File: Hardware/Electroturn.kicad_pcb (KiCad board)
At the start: 2 copper layers, 122 x 83.1 mm, 45 parts, among them Q1 2N2222, U2 RT9193-3.3, U3 74HC4050D

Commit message: Something like a pcb?
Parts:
- removed @HOLE0, @HOLE1, @HOLE2, @HOLE3: , 
- removed A0, A1, A2: , Adafruit 0.54 Alphanumeric v0.1:SOLDERJUMPER_REFLOW_NOPASTE
- removed C1: 10uF, Adafruit 0.54 Alphanumeric v0.1:0805-NO
- removed C1, C2, C3: 10uF, Adafruit_2.2_SPI_240x320:_0805MP
- removed CN1: , Adafruit_2.2_SPI_240x320:MICROSD
- removed D1: 1N4148, Adafruit 0.54 Alphanumeric v0.1:SOD-323F
- removed FID1, FID2, FID3: FIDUCIAL"", Adafruit_2.2_SPI_240x320:FIDUCIAL_1MM
- removed JP1: , Adafruit 0.54 Alphanumeric v0.1:1X05_ROUND_70
- removed JP1: , Adafruit_2.2_SPI_240x320:1X10_ROUND70
- removed LED1, LED2: , Adafruit 0.54 Alphanumeric v0.1:SEGMENT_STARTBUST_DUAL_KWA-541CBB
- removed Q1: 2N2222, Adafruit_2.2_SPI_240x320:SOT23-WIDE
- removed R1, R2: 10K, Adafruit 0.54 Alphanumeric v0.1:0805-NO
- removed R1, R2, R3, R6: 10, Adafruit_2.2_SPI_240x320:_0805MP
- removed R3, R4, R5: 47K, Adafruit 0.54 Alphanumeric v0.1:0805-NO
- removed R4: 1K, Adafruit_2.2_SPI_240x320:_0805MP
- removed R5: 10K, Adafruit_2.2_SPI_240x320:_0805MP
- removed U$1, U$2: FIDUCIAL, Adafruit 0.54 Alphanumeric v0.1:FIDUCIAL_1MM
- removed U$2, U$3, U$4, U$5: MOUNTINGHOLE2.5, Adafruit_2.2_SPI_240x320:MOUNTINGHOLE_2.5_PLATED
- removed U$20: , Adafruit_2.2_SPI_240x320:ADAFRUIT_TEXT_30MM
- removed U$3: , Adafruit 0.54 Alphanumeric v0.1:ADAFRUIT_9MM
- removed U1: , Adafruit_2.2_SPI_240x320:TM022HDH26_2.2IN_LCD
- removed U2: , Adafruit 0.54 Alphanumeric v0.1:SOP28_300MIL
- removed U2: RT9193-3.3, Adafruit_2.2_SPI_240x320:SOT23-5
- removed U3: 74HC4050D, Adafruit_2.2_SPI_240x320:SOIC16
- added REF**: Gecko G250x, Connector_PinSocket_2.54mm:PinSocket_2x15_P2.54mm_Vertical, F.Cu at (99.1, 78.7)
- added REF**: Alphanumeric, Connector_PinSocket_2.54mm:PinSocket_1x05_P2.54mm_Vertical, F.Cu at (121.9, 38.1)
- added REF**: Screw Terminal, TerminalBlock_Wuerth:Wuerth_REDCUBE-THR_WP-THRBU_74650194_THR, F.Cu at (118.0, 110.0)
- added REF**: 5k, Resistor_SMD:R_0402_1005Metric, F.Cu at (117.3, 56.6)
- added REF**: Screw Terminal, TerminalBlock_Wuerth:Wuerth_REDCUBE-THR_WP-THRBU_74650194_THR, F.Cu at (94.0, 45.7)
- added REF**: 10k, Resistor_SMD:R_0402_1005Metric, F.Cu at (107.2, 61.7)
- added REF**: 5k, Resistor_SMD:R_0402_1005Metric, F.Cu at (117.3, 61.6)
- added REF**: TFT Display, Connector_PinSocket_2.54mm:PinSocket_1x10_P2.54mm_Vertical, F.Cu at (172.1, 64.2)
- added REF**: 10k, Resistor_SMD:R_0402_1005Metric, F.Cu at (107.2, 56.6)
- added REF**: 2.8k, Resistor_SMD:R_0402_1005Metric, F.Cu at (89.5, 109.0)
- moved REF** 54.1 mm to (137.6, 77.2)
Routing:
- net (no net): track 1691.0 -> 1259.2 mm, vias 51 -> 40
- removed copper zone on F.Cu, net (none)
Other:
- board size 122 x 83.1 mm -> 100 x 100 mm
- board text removed: "+"
- board text removed: "-"
- board text removed: "0.54" 14-segment LED HT16K33 Backpack"
- board text removed: "240x320 2.2" TFT w/ILI9340C"
- board text removed: "A0"
- board text removed: "A1"
- board text removed: "A2"
- board text removed: "BACKLIGHT"
- board text removed: "BL"
- board text removed: "Backlight: PWM Safe"
- board text removed: "C"
- board text removed: "CS"
- board text removed: "D"
- board text removed: "D/C"
- board text removed: "GND"
- board text removed: "LCD CS"
- board text removed: "Logic: 3.3-5V"
- board text removed: "MISO"
- board text removed: "MOSI"
- board text removed: "RESET"
- board text removed: "RST"
- board text removed: "SCK"
- board text removed: "SCL"
- board text removed: "SD CS"
- board text removed: "SDA"
- board text removed: "SDCS"
- board text removed: "VCC"
- board text removed: "VIN"
- board text removed: "VIN: 3.3-5V"
- board text removed: "Vi2c"
- board text removed: "by adafruit!"

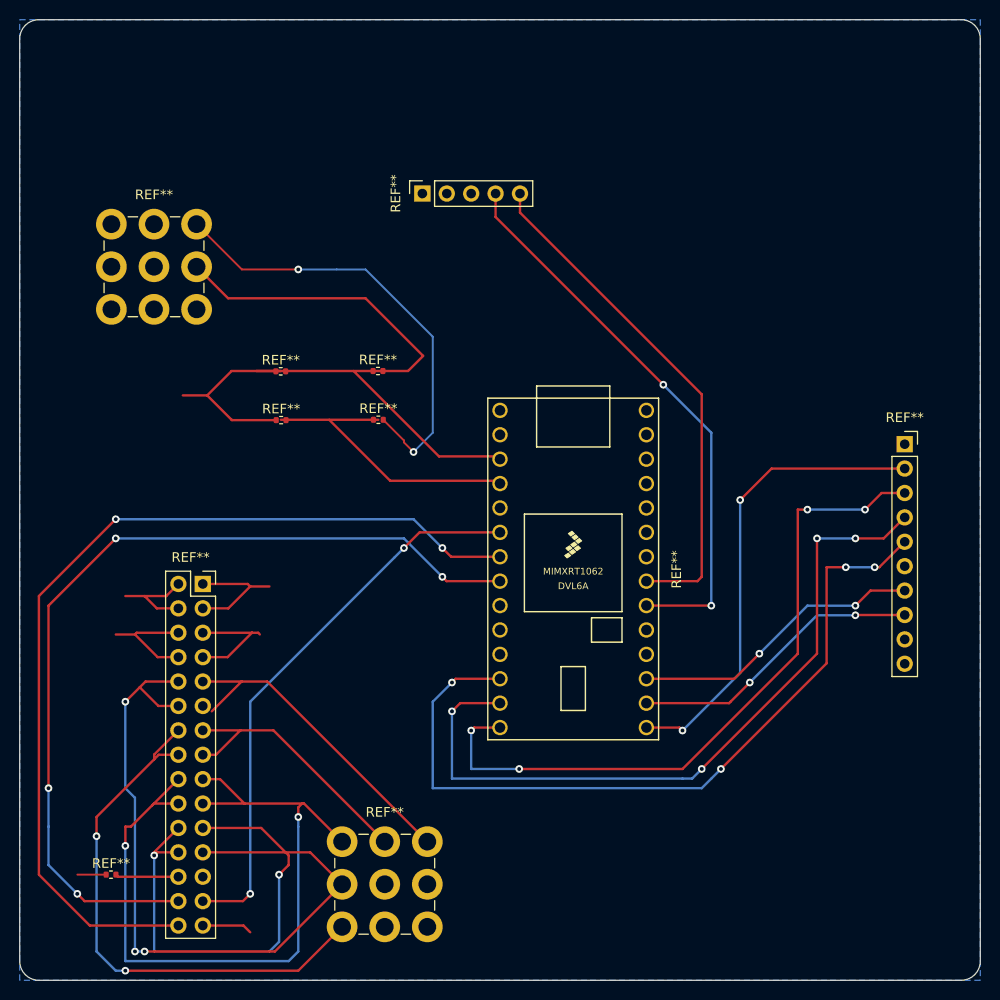
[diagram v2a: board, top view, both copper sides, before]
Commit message: Reorganizing KiCAD repo, fixing path issues
I tidied up the folder structure, and also went in and relinked all the footprints/symbols using the correct new paths. Should work across any system now. Also linked the appropriate 3D models for the Teensy and Gecko.
I updated the PCB to include all these new changes from the footprints/schematic, and in doing so it pretty much destroyed what Karson had...sorry Karson
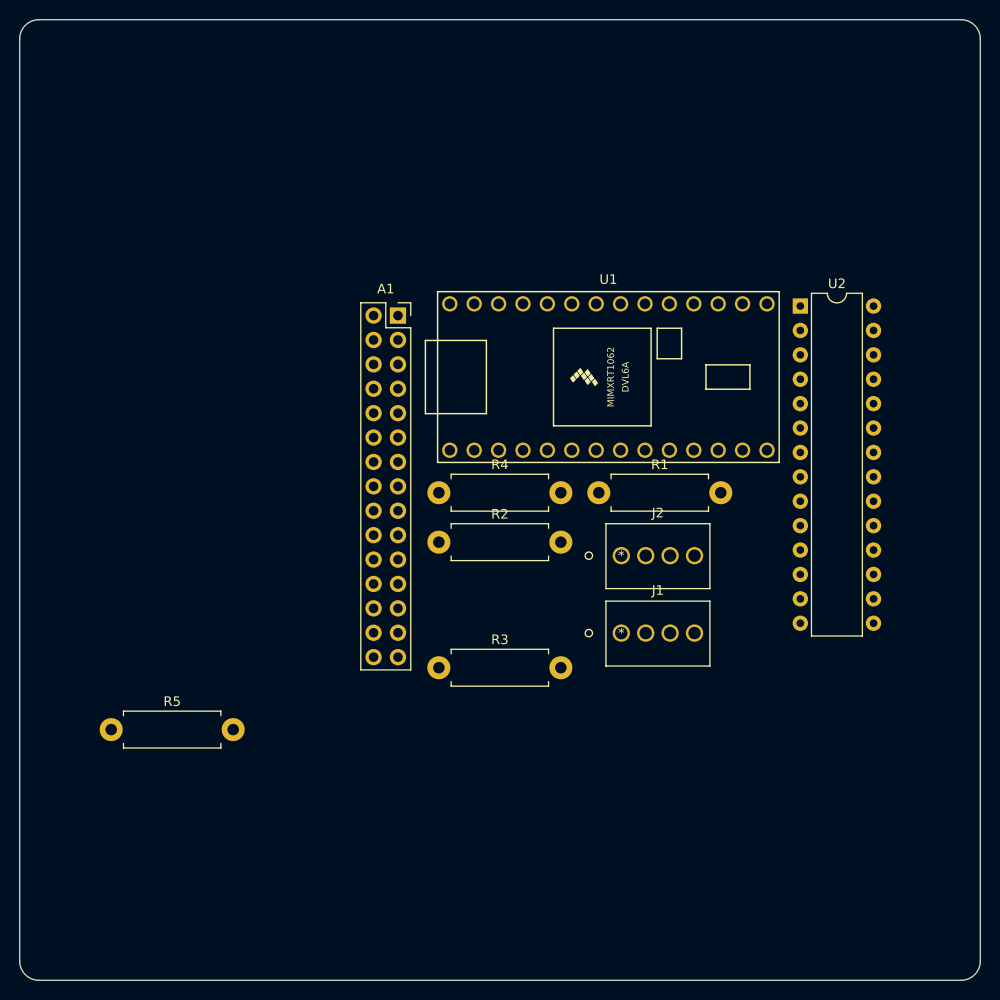
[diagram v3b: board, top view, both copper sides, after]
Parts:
- removed REF**: Gecko G250x, Connector_PinSocket_2.54mm:PinSocket_2x15_P2.54mm_Vertical
- removed REF**: Alphanumeric, Connector_PinSocket_2.54mm:PinSocket_1x05_P2.54mm_Vertical
- removed REF** (x2): Screw Terminal, TerminalBlock_Wuerth:Wuerth_REDCUBE-THR_WP-THRBU_74650194_THR
- removed REF** (x2): 5k, Resistor_SMD:R_0402_1005Metric
- removed REF** (x2): 10k, Resistor_SMD:R_0402_1005Metric
- removed REF**: TFT Display, Connector_PinSocket_2.54mm:PinSocket_1x10_P2.54mm_Vertical
- removed REF**: 2.8k, Resistor_SMD:R_0402_1005Metric
- removed REF**: Teensy 4.0, teensy:Teensy40
- added A1: Gecko G250X, Electroturn_Parts:GeckoG250XR2_WithHeatsink, F.Cu at (119.4, 50.8)
- added J1: Encoder Terminal, Electroturn_Parts:ScrewTerminal4_OSTVN04A150, F.Cu at (142.6, 83.9)
- added J2: Stepper Motor Terminal, Electroturn_Parts:ScrewTerminal4_OSTVN04A150, F.Cu at (142.6, 75.8)
- added R1: 10k, Resistor_THT:R_Axial_DIN0411_L9.9mm_D3.6mm_P12.70mm_Horizontal, F.Cu at (140.3, 69.2)
- added R2: 10k, Resistor_THT:R_Axial_DIN0411_L9.9mm_D3.6mm_P12.70mm_Horizontal, F.Cu at (123.6, 74.4)
- added R3: 5k, Resistor_THT:R_Axial_DIN0411_L9.9mm_D3.6mm_P12.70mm_Horizontal, F.Cu at (123.6, 87.5)
- added R4: 5k, Resistor_THT:R_Axial_DIN0411_L9.9mm_D3.6mm_P12.70mm_Horizontal, F.Cu at (123.6, 69.2)
- added R5: 2.8K, Resistor_THT:R_Axial_DIN0411_L9.9mm_D3.6mm_P12.70mm_Horizontal, F.Cu at (89.5, 93.9)
- added U1: Teensy 4.0, Electroturn_Parts:Teensy40_OnFemaleHeaders, F.Cu at (141.3, 57.2)
- added U2: MCP23017_SP, Package_DIP:DIP-28_W7.62mm, F.Cu at (161.3, 49.8)
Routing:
- net (no net): track 1259.2 -> 0.00 mm, vias 40 -> 0
- removed copper zone on B.Cu, net (none)

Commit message: Initial PCB work
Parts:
- added C1: 0.01uF, Capacitor_THT:C_Disc_D9.0mm_W5.0mm_P7.50mm, B.Cu at (195.8, 190.2)
- added C2: 0.01uF, Capacitor_THT:C_Disc_D9.0mm_W5.0mm_P7.50mm, B.Cu at (88.3, 159.4)
- added D1: Spindle Overspeed LED, LED_THT:LED_D5.0mm, F.Cu at (137.8, 73.7)
- added DS1: Adafruit_1002_Alphanumeric, Electroturn_Parts:Adafruit1002_0.54inAlphanumericBackpack, F.Cu at (121.9, 39.6)
- added DS2: Adafruit_1480_2.2inTFT, Electroturn_Parts:Adafruit1480_TFTwithHeaders, F.Cu at (160.7, 112.1)
- added R10: 10k, Resistor_THT:R_Axial_DIN0411_L9.9mm_D3.6mm_P12.70mm_Horizontal, B.Cu at (59.8, 147.3)
- added R11: 10k, Resistor_THT:R_Axial_DIN0411_L9.9mm_D3.6mm_P12.70mm_Horizontal, B.Cu at (177.3, 163.8)
- added R6: 1.5k, Resistor_THT:R_Axial_DIN0411_L9.9mm_D3.6mm_P12.70mm_Horizontal, B.Cu at (177.3, 168.9)
- added R7: 1.5k, Resistor_THT:R_Axial_DIN0411_L9.9mm_D3.6mm_P12.70mm_Horizontal, B.Cu at (195.6, 184.4)
- added R8: 10k, Resistor_THT:R_Axial_DIN0411_L9.9mm_D3.6mm_P12.70mm_Horizontal, B.Cu at (133.3, 159.3)
- added R9: 10k, Resistor_THT:R_Axial_DIN0411_L9.9mm_D3.6mm_P12.70mm_Horizontal, B.Cu at (177.3, 148.3)
- added SW1: Feed Switch, Electroturn_Parts:SPDT_OnOffOn_ToggleSwitch_fromECEdepartment_CircularPads, F.Cu at (91.1, 112.8)
- added SW2: Motor Braking Switch, Electroturn_Parts:SW_SPDT_CK_ A11405RNZQ, F.Cu at (97.8, 84.5)
- added SW3: Mode Right Scroll, Button_Switch_THT:SW_PUSH_6mm, F.Cu at (183.4, 39.7)
- added SW4: Mode Left Scroll, Button_Switch_THT:SW_PUSH_6mm, F.Cu at (154.9, 39.7)
- added SW5: Function Btn 1, Button_Switch_THT:SW_PUSH_6mm, F.Cu at (199.3, 80.3)
- added SW6: Function Btn 2, Button_Switch_THT:SW_PUSH_6mm, F.Cu at (199.3, 90.5)
- added SW7: Function Btn 2, Button_Switch_THT:SW_PUSH_6mm, F.Cu at (199.3, 100.0)
- added SW8: Control Panel Encoder, Electroturn_Parts:CUIDevices_ACZ11BR1E20FD112C, F.Cu at (203.2, 63.5)
- A1, J1, J2, R1, R2, R4, U1, U2: moved to B.Cu
- R3: value 5k -> 2.8K; moved to B.Cu
- R5: value 2.8K -> 5k; moved to B.Cu
- moved U1 134.1 mm to (236.3, 151.8), turned to 180 degrees
- moved J1 110.2 mm to (57.5, 153.9), turned to 180 degrees
- moved A1 109.8 mm to (181.6, 141.3), turned to 180 degrees
- moved R5 109.1 mm to (177.3, 158.6), turned to 180 degrees
- moved J2 104.8 mm to (175.0, 175.5), turned to 180 degrees
- moved U2 91.4 mm to (115.9, 129.2), turned to 180 degrees
- moved R4 91.4 mm to (104.7, 158.7), turned to 180 degrees
- moved R2 87.3 mm to (160.7, 153.5), turned to 180 degrees
- moved R3 85.1 mm to (177.3, 153.5), turned to 180 degrees
- moved R1 81.7 mm to (160.7, 148.3), turned to 180 degrees
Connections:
- R3 pad 1: Net-(R1-Pad2) -> Net-(A1-Pad25)
- R3 pad 2: /SpindleEnc_A -> GND
- R4 pad 1: Net-(R2-Pad2) -> Net-(R1-Pad2)
- R4 pad 2: /SpindleEnc_B -> /SpindleEnc_A
- R5 pad 1: Net-(A1-Pad25) -> Net-(R2-Pad2)
- R5 pad 2: GND -> /SpindleEnc_B
- U2 pad 15: unconnected-(U2-Pad15) -> GND
- U2 pad 16: unconnected-(U2-Pad16) -> GND
- U2 pad 17: unconnected-(U2-Pad17) -> GND
- U2 pad 18: unconnected-(U2-Pad18) -> +3V3
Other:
- board size 100 x 100 mm -> 133.3 x 82.5 mm

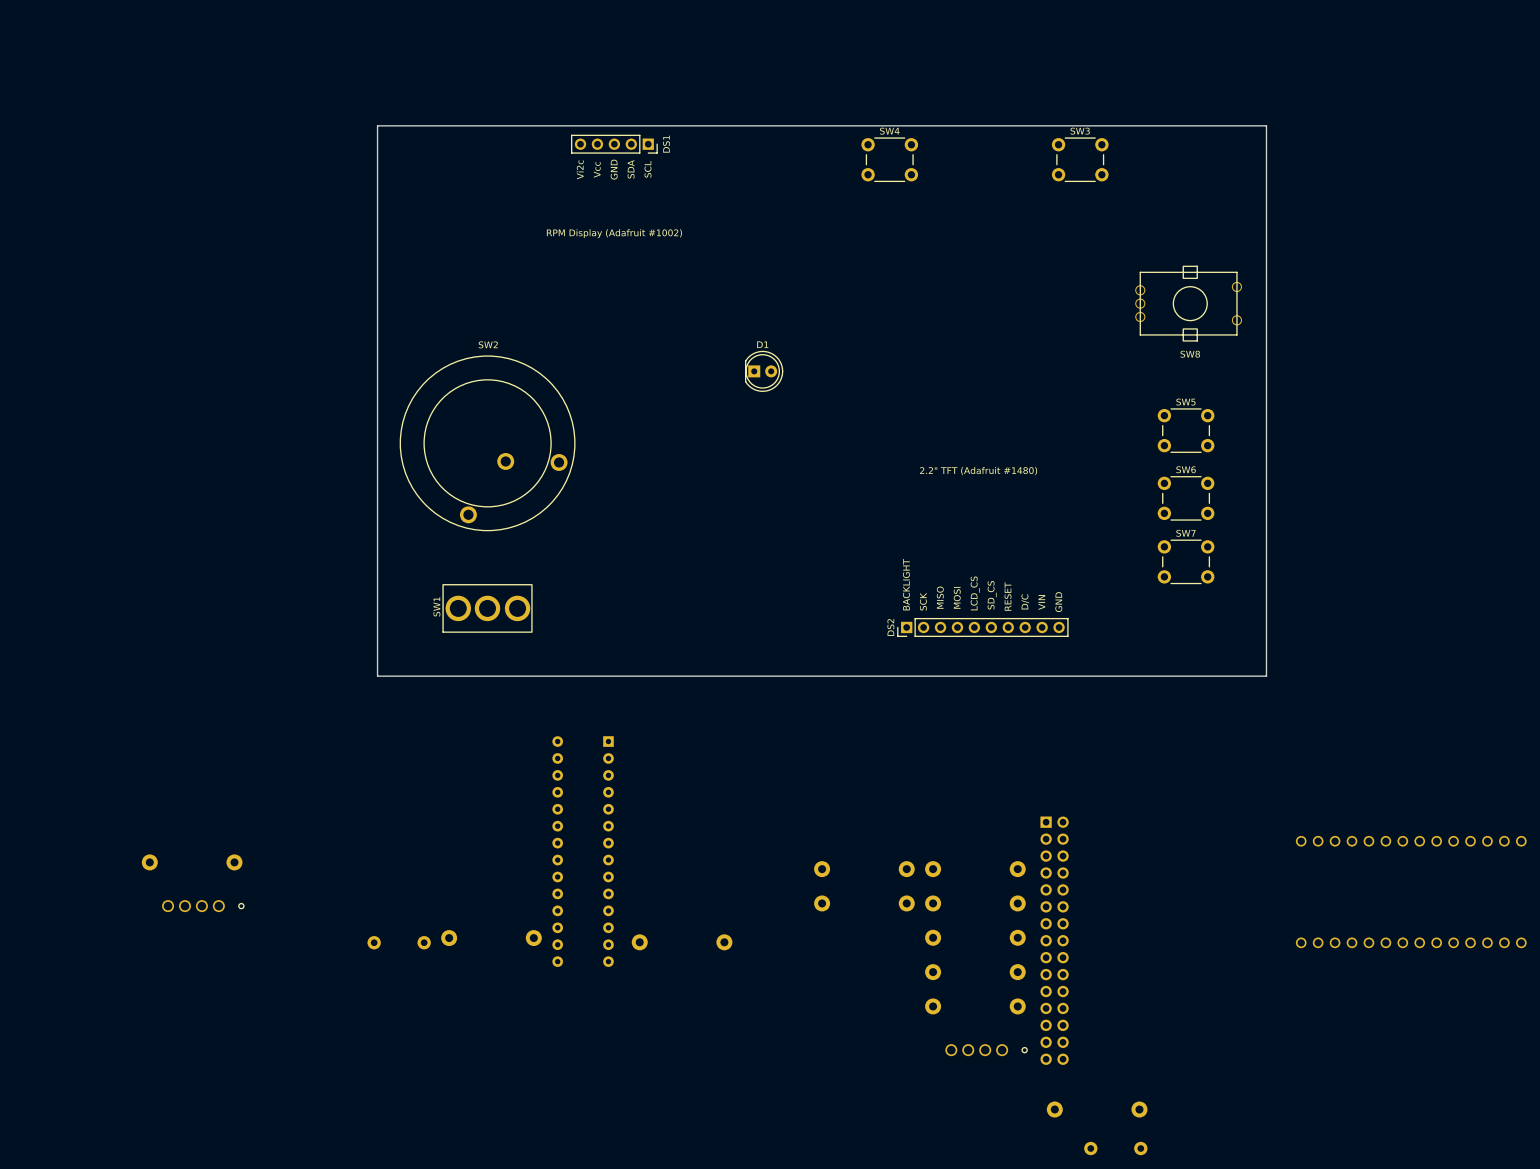
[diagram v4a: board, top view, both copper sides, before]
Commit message: Revert "Initial PCB work" to prevent KiCad merge hell
This reverts commit 830c4b3218d3f5d7a4b251521e18afe8c7a9bcf8.
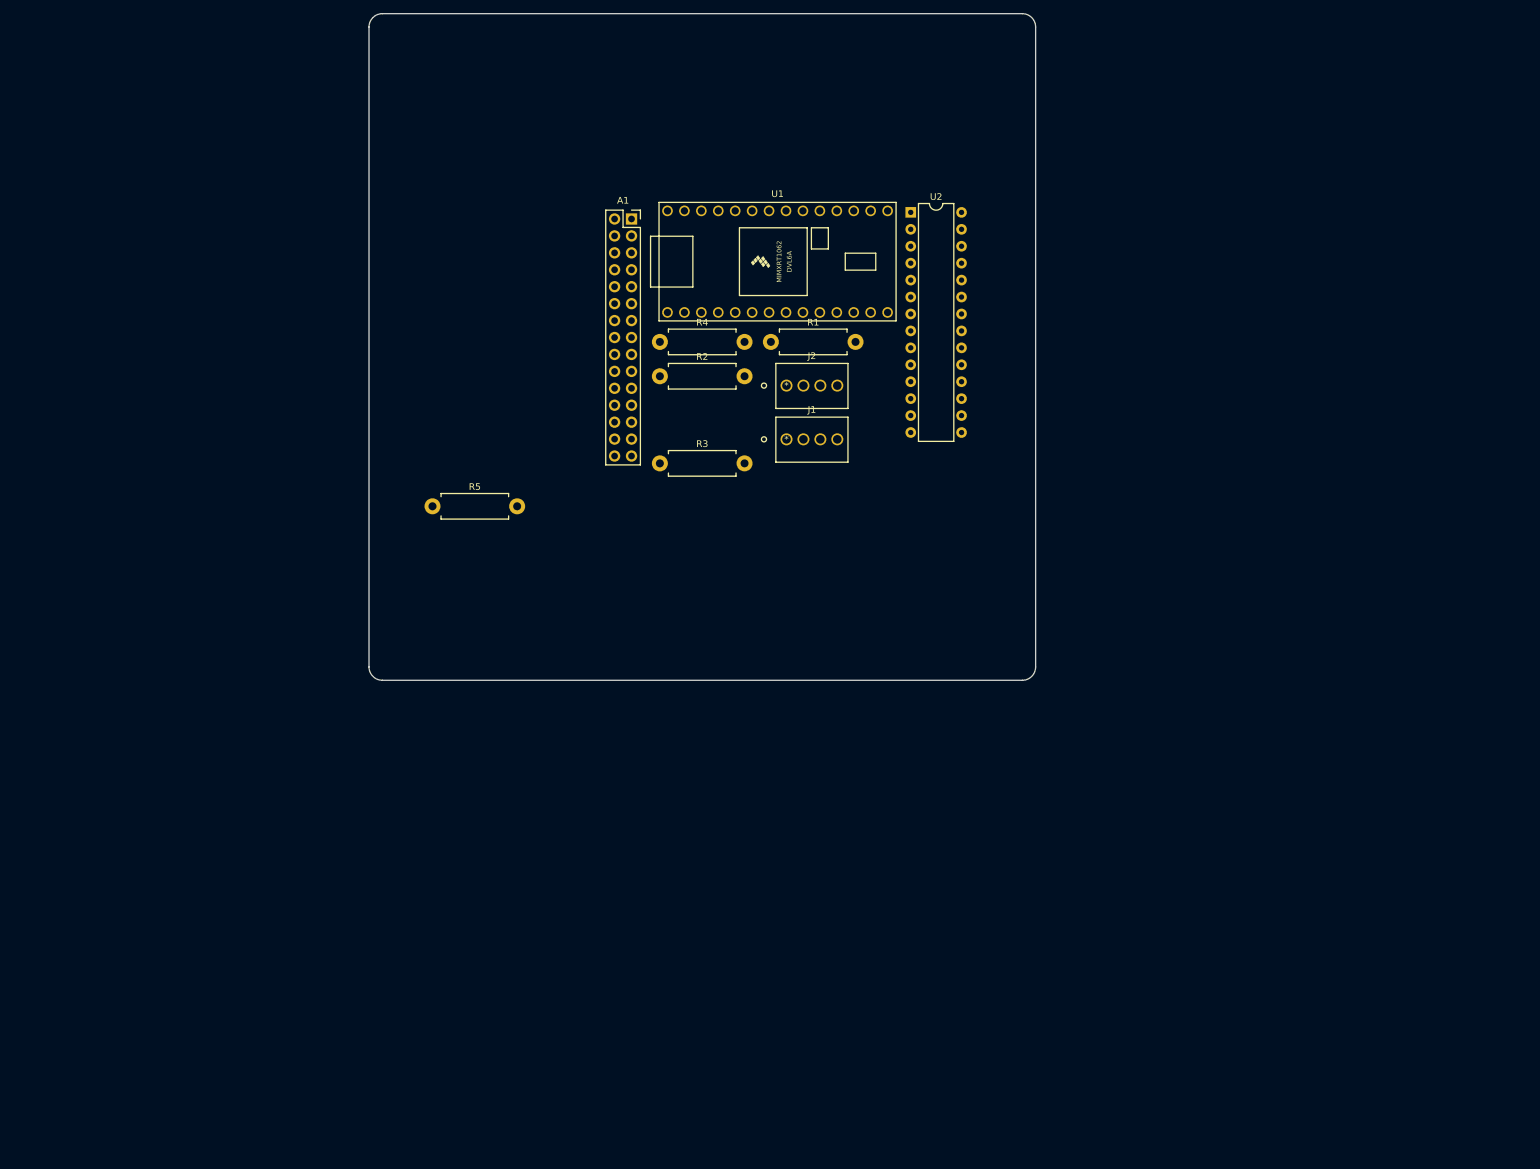
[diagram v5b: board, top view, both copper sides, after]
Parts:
- removed C1, C2: 0.01uF, Capacitor_THT:C_Disc_D9.0mm_W5.0mm_P7.50mm
- removed D1: Spindle Overspeed LED, LED_THT:LED_D5.0mm
- removed DS1: Adafruit_1002_Alphanumeric, Electroturn_Parts:Adafruit1002_0.54inAlphanumericBackpack
- removed DS2: Adafruit_1480_2.2inTFT, Electroturn_Parts:Adafruit1480_TFTwithHeaders
- removed R10, R11, R8, R9: 10k, Resistor_THT:R_Axial_DIN0411_L9.9mm_D3.6mm_P12.70mm_Horizontal
- removed R6, R7: 1.5k, Resistor_THT:R_Axial_DIN0411_L9.9mm_D3.6mm_P12.70mm_Horizontal
- removed SW1: Feed Switch, Electroturn_Parts:SPDT_OnOffOn_ToggleSwitch_fromECEdepartment_CircularPads
- removed SW2: Motor Braking Switch, Electroturn_Parts:SW_SPDT_CK_ A11405RNZQ
- removed SW3: Mode Right Scroll, Button_Switch_THT:SW_PUSH_6mm
- removed SW4: Mode Left Scroll, Button_Switch_THT:SW_PUSH_6mm
- removed SW5: Function Btn 1, Button_Switch_THT:SW_PUSH_6mm
- removed SW6, SW7: Function Btn 2, Button_Switch_THT:SW_PUSH_6mm
- removed SW8: Control Panel Encoder, Electroturn_Parts:CUIDevices_ACZ11BR1E20FD112C
- A1, J1, J2, R1, R2, R4, U1, U2: moved to F.Cu
- R3: value 2.8K -> 5k; moved to F.Cu
- R5: value 5k -> 2.8K; moved to F.Cu
- moved U1 134.1 mm to (141.3, 57.2), turned to 0 degrees
- moved J1 110.2 mm to (142.6, 83.9), turned to 0 degrees
- moved A1 109.8 mm to (119.4, 50.8), turned to 0 degrees
- moved R5 109.1 mm to (89.5, 93.9), turned to 0 degrees
- moved J2 104.8 mm to (142.6, 75.8), turned to 0 degrees
- moved U2 91.4 mm to (161.3, 49.8), turned to 0 degrees
- moved R4 91.4 mm to (123.6, 69.2), turned to 0 degrees
- moved R2 87.3 mm to (123.6, 74.4), turned to 0 degrees
- moved R3 85.1 mm to (123.6, 87.5), turned to 0 degrees
- moved R1 81.7 mm to (140.3, 69.2), turned to 0 degrees
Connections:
- R3 pad 1: Net-(A1-Pad25) -> Net-(R1-Pad2)
- R3 pad 2: GND -> /SpindleEnc_A
- R4 pad 1: Net-(R1-Pad2) -> Net-(R2-Pad2)
- R4 pad 2: /SpindleEnc_A -> /SpindleEnc_B
- R5 pad 1: Net-(R2-Pad2) -> Net-(A1-Pad25)
- R5 pad 2: /SpindleEnc_B -> GND
- U2 pad 15: GND -> unconnected-(U2-Pad15)
- U2 pad 16: GND -> unconnected-(U2-Pad16)
- U2 pad 17: GND -> unconnected-(U2-Pad17)
- U2 pad 18: +3V3 -> unconnected-(U2-Pad18)
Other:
- board size 133.3 x 82.5 mm -> 100 x 100 mm
